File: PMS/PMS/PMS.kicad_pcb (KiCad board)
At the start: 4 copper layers, 82.5 x 57.5 mm, 32 parts, among them IC1 TMCS1107A1BQDRQ1, IC2 ADR3450ARJZ-R7, J1 XT60PW-M, J2 XT60PW-F, J3 XT60PW-M, J4 XT60PW-F, J5 XT60PW-F, J6 Conn_01x03_Male, J7 Conn_01x02_Male, U1 ADC101C027CIMK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

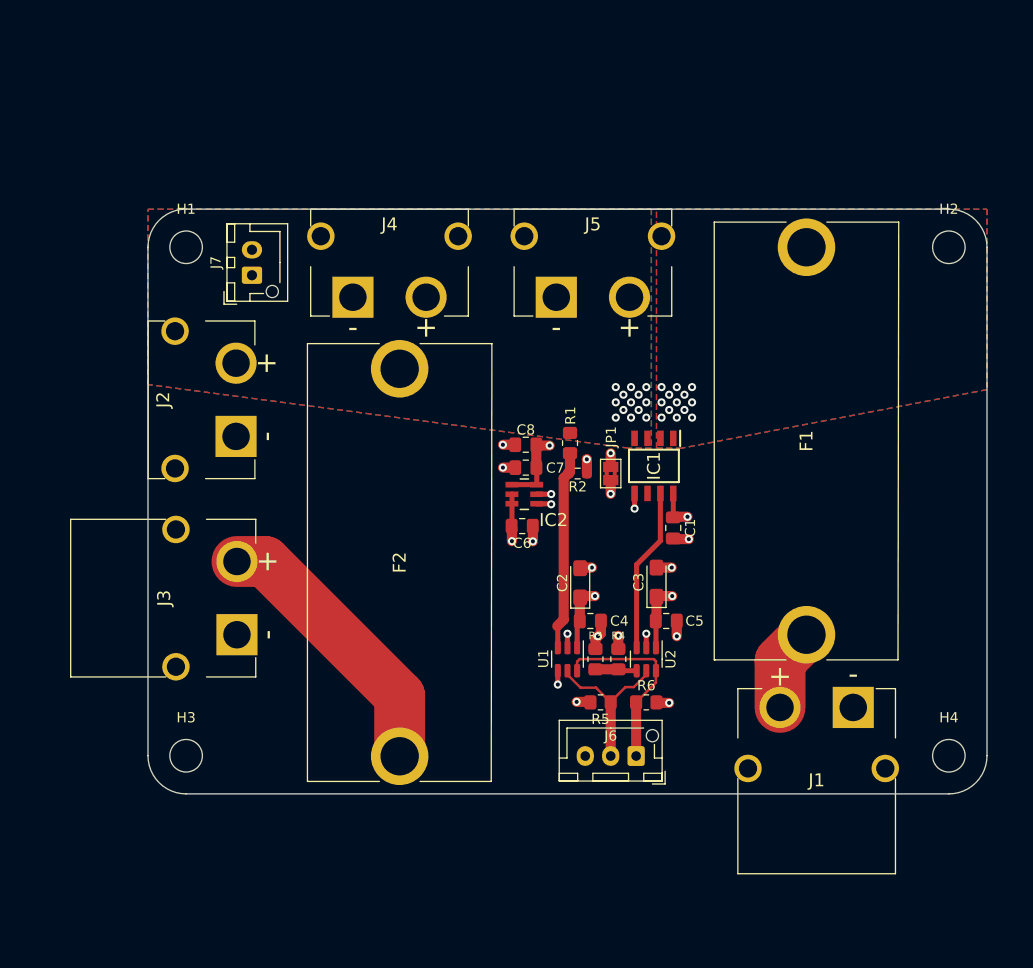
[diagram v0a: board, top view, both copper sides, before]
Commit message: Changed regulator and updated layout. No longer includes LA12.
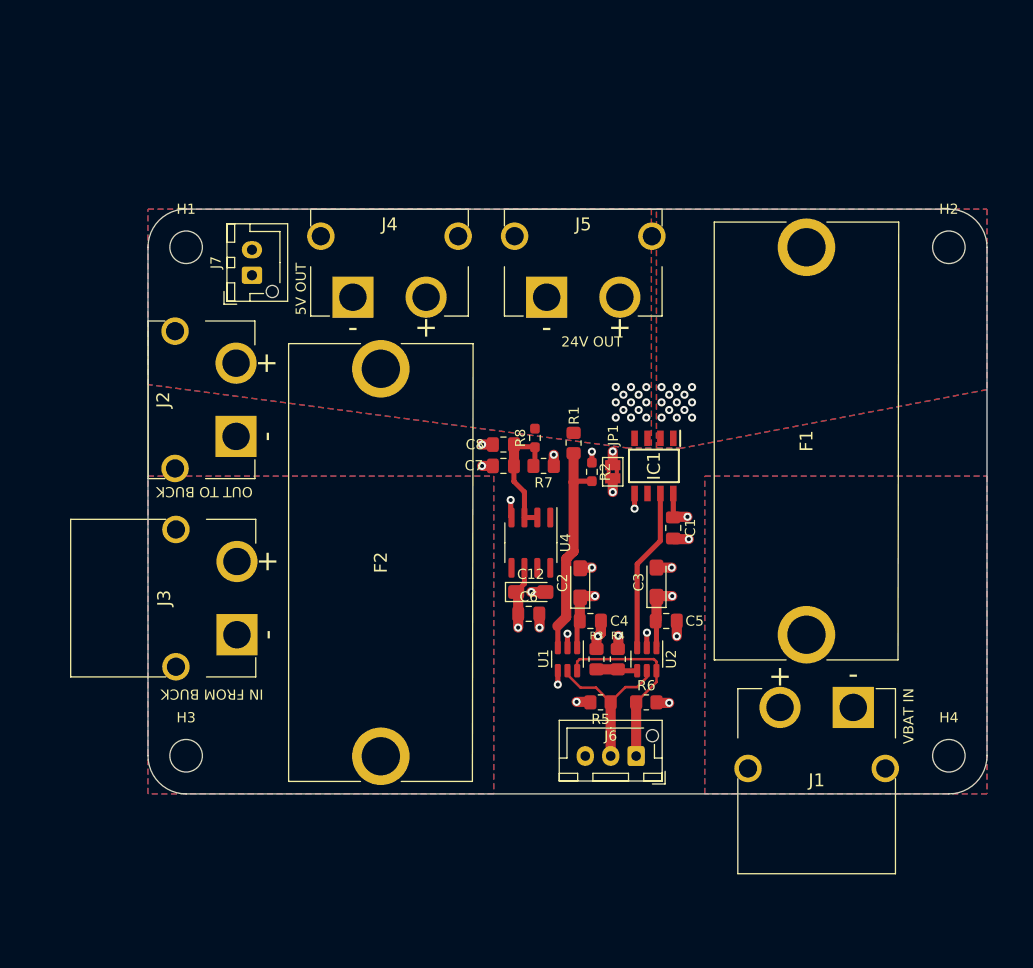
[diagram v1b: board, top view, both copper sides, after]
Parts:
- removed IC2: ADR3450ARJZ-R7, ADR3450ARJZ-R7:SOT95P280X145-6N
- added C12: 1 uF, Capacitor_Tantalum_SMD:CP_EIA-3216-18_Kemet-A_Pad1.58x1.35mm_HandSolder, F.Cu at (93.9, 85.9)
- added R7: 1M, Resistor_SMD:R_0805_2012Metric_Pad1.20x1.40mm_HandSolder, F.Cu at (95.2, 73.5)
- added R8: 2M, Resistor_SMD:R_0603_1608Metric_Pad0.98x0.95mm_HandSolder, F.Cu at (94.3, 70.8)
- added U4: REF195, Package_SO:SOIC-8_3.9x4.9mm_P1.27mm, F.Cu at (93.9, 81.0)
- C8: value 1uF -> 10uF
- moved C6 8.65 mm to (93.7, 88.0), turned to 0 degrees
- moved C7 2.21 mm to (91.2, 73.5), turned to 0 degrees
- moved C8 2.20 mm to (91.2, 71.4)
- moved F2 1.85 mm to (79.2, 102.0)
- moved R2 1.41 mm to (99.9, 74.1), turned to 90 degrees
- moved J5 0.95 mm to (99.0, 56.9)
- moved R1 0.35 mm to (98.1, 71.2)
- moved JP1 0.27 mm to (102.0, 74.1)
- moved R3 0.10 mm to (100.3, 92.5)
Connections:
- C6 pad 1: GNDA -> +5VA
- C6 pad 2: +5VA -> GNDA
- C7 pad 1: +5V -> GND
- C7 pad 2: GND -> Net-(C7-Pad2)
- C8 pad 1: +5V -> Net-(C7-Pad2)
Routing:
- net +5VP: track 27.4 -> 0.00 mm
- net Net-(C7-Pad2): track 0.00 -> 12.1 mm
- net +BATT: track 8.23 -> 0.00 mm
- net +5V: track 7.55 -> 0.00 mm, vias 1 -> 0
- net Net-(R1-Pad2): track 19.7 -> 21.6 mm
- net +5VA: track 24.3 -> 26.0 mm
- net GND: track 5.18 -> 5.65 mm, vias 4 -> 5
- added copper zone on B.Cu, net +5VP
- added copper zone on F.Cu, net +5VP
- added copper zone on In2.Cu, net +5VP
- added copper zone on B.Cu, net +BATT
- added copper zone on F.Cu, net +BATT
- added copper zone on In2.Cu, net +BATT
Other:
- board text added: "24V OUT"
- board text added: "5V OUT"
- board text added: "IN FROM BUCK"
- board text added: "OUT TO BUCK"
- board text added: "VBAT IN"

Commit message: updates to satisfy DRC
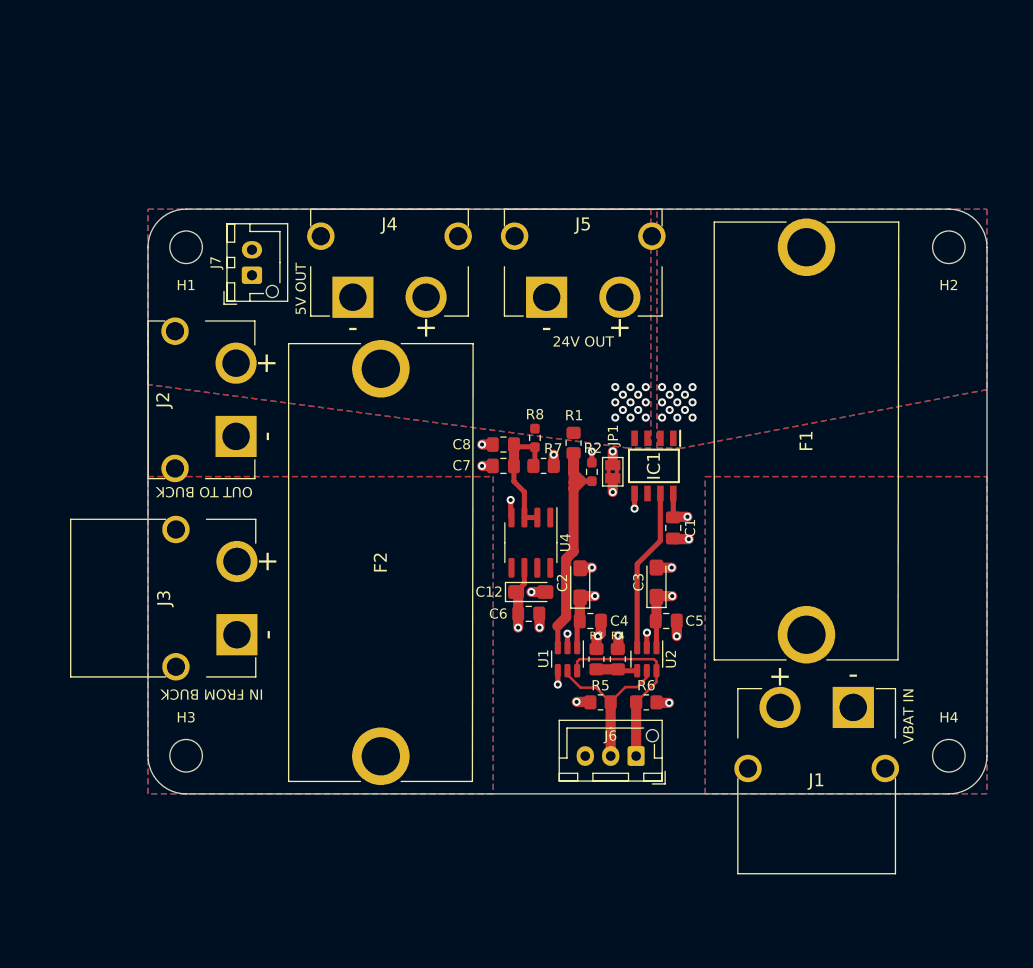
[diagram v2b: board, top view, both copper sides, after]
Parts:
- turned H1 to 180 degrees
- turned H2 to 180 degrees
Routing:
- net Net-(R1-Pad2): track 21.6 -> 25.8 mm

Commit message: changed solder jumper footprint and added silk labels for XT60 connectors
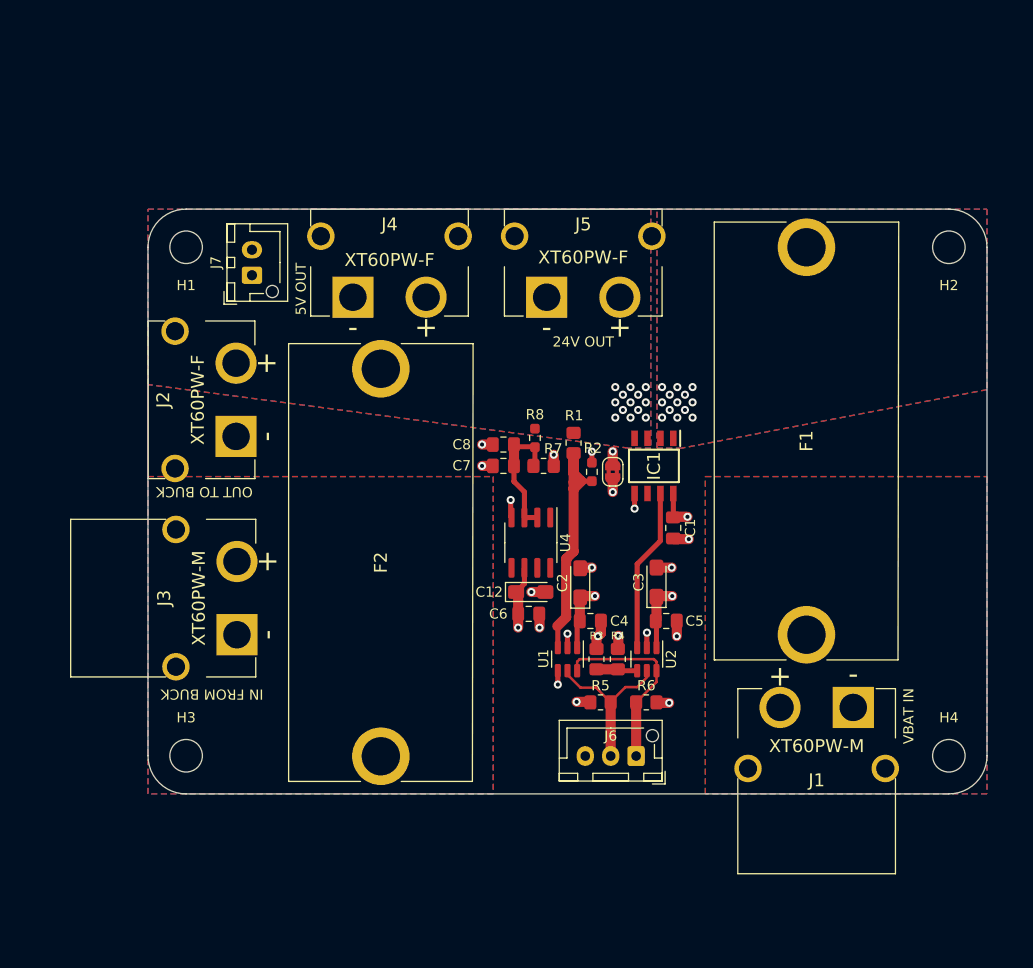
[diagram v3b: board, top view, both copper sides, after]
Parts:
- JP1: footprint Jumper:SolderJumper-2_P1.3mm_Bridged2Bar_Pad1.0x1.5mm -> Jumper:SolderJumper-2_P1.3mm_Bridged2Bar_RoundedPad1.0x1.5mm
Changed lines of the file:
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@@
       (effects (font (size 1.27 1.27) (thickness 0.254)))
     )
-    (fp_text value "XT60PW-F" (at 0 -7.163 90) (layer "F.SilkS") hide
+    (fp_text value "XT60PW-F" (at 0 -3.7625 90) (layer "F.SilkS")
       (effects (font (size 1.27 1.27) (thickness 0.254)))
     )
@@
       (effects (font (size 1.27 1.27) (thickness 0.254)))
     )
-    (fp_text value "XT60PW-M" (at 0 -7.163) (layer "F.SilkS") hide
+    (fp_text value "XT60PW-M" (at 0 -3.8 180) (layer "F.SilkS")
       (effects (font (size 1.27 1.27) (thickness 0.254)))
     )
@@
       (effects (font (size 1.27 1.27) (thickness 0.254)))
     )
-    (fp_text value "XT60PW-F" (at 0 -7.163) (layer "F.SilkS") hide
+    (fp_text value "XT60PW-F" (at 0 -3.6625) (layer "F.SilkS")
       (effects (font (size 1.27 1.27) (thickness 0.254)))
     )
@@
     )
   )
-  (footprint "Jumper:SolderJumper-2_P1.3mm_Bridged2Bar_Pad1.0x1.5mm" (layer "F.Cu")
+  (footprint "Jumper:SolderJumper-2_P1.3mm_Bridged2Bar_RoundedPad1.0x1.5mm" (layer "F.Cu")
     (at 101.95 74.075 -90)
-    (descr "SMD Solder Jumper, 1x1.5mm Pads, 0.3mm gap, bridged with 2 copper strips")
+    (descr "SMD Solder Jumper, 1x1.5mm, rounded Pads, 0.3mm gap, bridged with 2 copper strips")
     (tags "net tie solder jumper bridged")
     (property "Sheetfile" "PMS.kicad_sch")
     (property "Sheetname" "")
     (attr exclude_from_pos_files)
-    (fp_text reference "JP1" (at -3.6 -0.05 90) (layer "F.SilkS")
-      (effects (font (size 1 1) (thickness 0.15)))
-    )
-    (fp_text value "Jumper_2_Bridged" (at 0 1.9 90) (layer "F.Fab")
-      (effects (font (size 1 1) (thickness 0.15)))
-    )
+    (fp_text reference "JP1" (at 0 -1.8 -90) (layer "F.SilkS") hide
+      (effects (font (size 1 1) (thickness 0.15)))
+    )
+    (fp_text value "Jumper_2_Bridged" (at 0 1.9 -90) (layer "F.Fab")
+      (effects (font (size 1 1) (thickness 0.15)))
+    )
+    (fp_poly (pts
+        (xy -0.25 0.2)
+        (xy 0.25 0.2)
+        (xy 0.25 0.6)
+        (xy -0.25 0.6)
+      ) (layer "F.Cu") (width 0) (fill solid))
     (fp_poly (pts
         (xy -0.25 -0.6)
@@
         (xy -0.25 -0.2)
       ) (layer "F.Cu") (width 0) (fill solid))
-    (fp_poly (pts
-        (xy -0.25 0.2)
-        (xy 0.25 0.2)
-        (xy 0.25 0.6)
-        (xy -0.25 0.6)
-      ) (layer "F.Cu") (width 0) (fill solid))
-    (fp_line (start 1.4 1) (end -1.4 1) (layer "F.SilkS") (width 0.12))
-    (fp_line (start -1.4 1) (end -1.4 -1) (layer "F.SilkS") (width 0.12))
-    (fp_line (start 1.4 -1) (end 1.4 1) (layer "F.SilkS") (width 0.12))
-    (fp_line (start -1.4 -1) (end 1.4 -1) (layer "F.SilkS") (width 0.12))
+    (fp_line (start -0.7 -1) (end 0.7 -1) (layer "F.SilkS") (width 0.12))
+    (fp_line (start -1.4 0.3) (end -1.4 -0.3) (layer "F.SilkS") (width 0.12))
+    (fp_line (start 0.7 1) (end -0.7 1) (layer "F.SilkS") (width 0.12))
+    (fp_line (start 1.4 -0.3) (end 1.4 0.3) (layer "F.SilkS") (width 0.12))
+    (fp_arc (start -0.7 1) (mid -1.194975 0.794975) (end -1.4 0.3) (layer "F.SilkS") (width 0.12))
+    (fp_arc (start 1.4 0.3) (mid 1.194975 0.794975) (end 0.7 1) (layer "F.SilkS") (width 0.12))
+    (fp_arc (start 0.7 -1) (mid 1.194975 -0.794975) (end 1.4 -0.3) (layer "F.SilkS") (width 0.12))
+    (fp_arc (start -1.4 -0.3) (mid -1.194975 -0.794975) (end -0.7 -1) (layer "F.SilkS") (width 0.12))
     (fp_line (start 1.65 1.25) (end 1.65 -1.25) (layer "F.CrtYd") (width 0.05))
     (fp_line (start -1.65 -1.25) (end 1.65 -1.25) (layer "F.CrtYd") (width 0.05))
     (fp_line (start 1.65 1.25) (end -1.65 1.25) (layer "F.CrtYd") (width 0.05))
     (fp_line (start -1.65 -1.25) (end -1.65 1.25) (layer "F.CrtYd") (width 0.05))
-    (pad "1" smd rect locked (at -0.65 0 270) (size 1 1.5) (layers "F.Cu" "F.Mask")
-      (net 2 "GND") (pinfunction "A") (pintype "passive"))
-    (pad "2" smd rect locked (at 0.65 0 270) (size 1 1.5) (layers "F.Cu" "F.Mask")
-      (net 15 "GNDA") (pinfunction "B") (pintype "passive"))
+    (pad "1" smd custom (at -0.65 0 270) (size 1 0.5) (layers "F.Cu" "F.Mask")
+      (net 2 "GND") (pinfunction "A") (pintype "passive") (zone_connect 2)
+      (options (clearance outline) (anchor rect))
+      (primitives
+        (gr_circle (center 0 0.25) (end 0.5 0.25) (width 0) (fill yes))
+        (gr_circle (center 0 -0.25) (end 0.5 -0.25) (width 0) (fill yes))
+        (gr_poly (pts
+            (xy 0.5 0.75)
+            (xy 0 0.75)
+            (xy 0 -0.75)
+            (xy 0.5 -0.75)
+          ) (width 0) (fill yes))
+      ))
+    (pad "2" smd custom (at 0.65 0 270) (size 1 0.5) (layers "F.Cu" "F.Mask")
+      (net 15 "GNDA") (pinfunction "B") (pintype "passive") (zone_connect 2)
+      (options (clearance outline) (anchor rect))
+      (primitives
+        (gr_circle (center 0 0.25) (end 0.5 0.25) (width 0) (fill yes))
+        (gr_circle (center 0 -0.25) (end 0.5 -0.25) (width 0) (fill yes))
+        (gr_poly (pts
+            (xy 0 0.75)
+            (xy -0.5 0.75)
+            (xy -0.5 -0.75)
+            (xy 0 -0.75)
+          ) (width 0) (fill yes))
+      ))
   )
   (footprint "MountingHole:MountingHole_3.2mm_M3_ISO14580" (layer "F.Cu")
@@
       (effects (font (size 1.27 1.27) (thickness 0.254)))
     )
-    (fp_text value "XT60PW-M" (at 0 -7.163 90) (layer "F.SilkS") hide
+    (fp_text value "XT60PW-M" (at 0 -3.75 90) (layer "F.SilkS")
       (effects (font (size 1.27 1.27) (thickness 0.254)))
     )
@@
       (effects (font (size 1.27 1.27) (thickness 0.254)))
     )
-    (fp_text value "XT60PW-F" (at 0 -7.163) (layer "F.SilkS") hide
-      (effects (font (size 1.27 1.27) (thickness 0.254)))
-    )
+    (fp_text value "XT60PW-F" (at 0 -3.9125) (layer "F.SilkS")
+      (effects (font (size 1.27 1.27) (thickness 0.254)))
+    )

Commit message: changed to XT90s for 24V
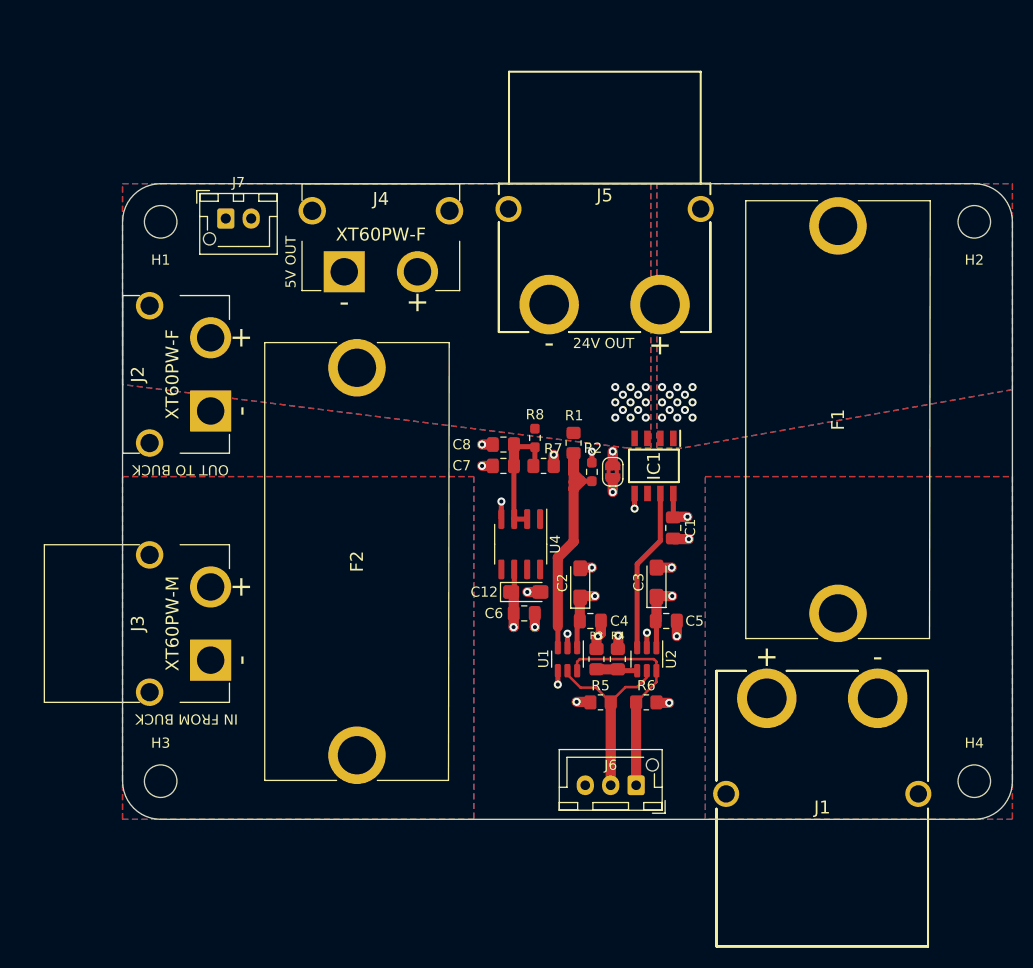
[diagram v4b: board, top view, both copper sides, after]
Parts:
- J1: value XT60PW-M -> XT90PW-M; footprint LIB_XT60PW-M:XT60PWM -> XT90PW-M:XT90PWM
- J5: value XT60PW-F -> XT90PWM; footprint LIB_XT60PW-F:XT60PWF -> XT90PW-F:XT90PW-F
- moved J5 7.58 mm to (106.6, 57.6), turned to 180 degrees
- moved J7 6.14 mm to (63.9, 49.2), turned to 0 degrees
- moved J1 4.98 mm to (117.1, 96.4), turned to 0 degrees
- moved F1 3.74 mm to (124.1, 88.0)
- moved J3 3.60 mm to (62.4, 89.0)
- moved H1 3.54 mm to (57.5, 49.5)
- moved H2 3.54 mm to (137.5, 49.5)
- moved H3 3.54 mm to (57.5, 104.5)
- moved H4 3.54 mm to (137.5, 104.5)
- moved J2 3.54 mm to (62.4, 64.5)
- moved J6 2.88 mm to (104.2, 104.9)
- moved J4 2.64 mm to (79.2, 54.4)
- moved F2 2.35 mm to (76.8, 102.0)
- moved U4 1.01 mm to (92.9, 81.2)
- moved C12 0.49 mm to (93.4, 85.9)
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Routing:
- net SCL: track 15.5 -> 18.3 mm
- net SDA: track 19.0 -> 21.9 mm
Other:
- board size 82.5 x 57.5 mm -> 87.5 x 62.5 mm
- board text removed: "VBAT IN"

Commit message: Changed to barrier strip for connection to Mean-Well. Interconnects cannot be erroneously connected
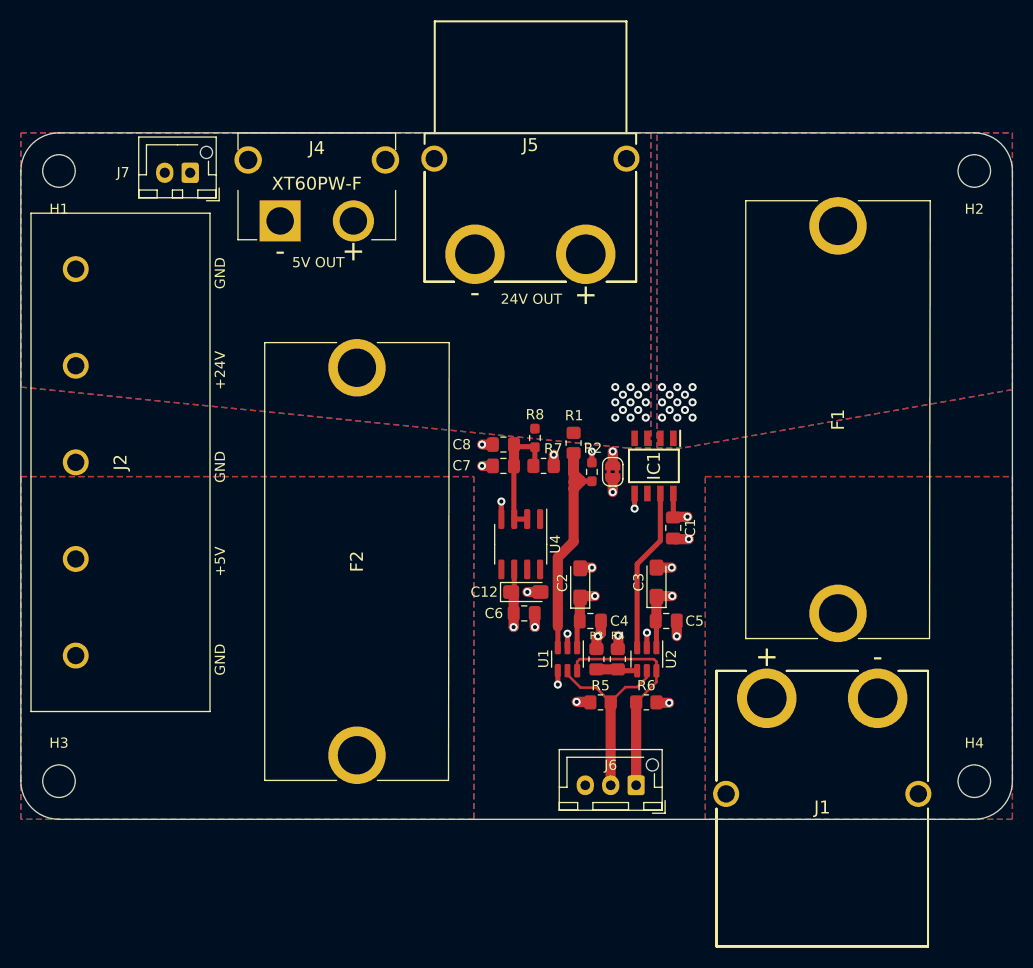
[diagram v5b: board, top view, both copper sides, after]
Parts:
- removed J3: XT60PW-M, LIB_XT60PW-M:XT60PWM
- J2: value XT60PW-F -> OSTYK44105030; footprint LIB_XT60PW-F:XT60PWF -> LIB_OSTYK44105030:OSTYK44105030
- moved J2 16.8 mm to (49.1, 54.1), turned to -90 degrees
- moved H1 11.2 mm to (47.5, 44.5)
- moved H3 10.0 mm to (47.5, 104.5)
- moved J5 8.82 mm to (99.3, 52.7)
- moved J4 8.04 mm to (72.8, 49.4)
- moved J7 5.70 mm to (60.4, 44.7), turned to 180 degrees
- moved H2 5.00 mm to (137.5, 44.5)
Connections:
- J2 pad 4: GND -> +5VP
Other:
- board size 87.5 x 62.5 mm -> 97.5 x 67.5 mm
- board text added: "+24V"
- board text added: "+5V"
- board text added: "GND"
- board text removed: "IN FROM BUCK"
- board text removed: "OUT TO BUCK"
